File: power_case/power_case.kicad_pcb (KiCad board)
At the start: 2 copper layers, 22 x 27.1 mm, 4 parts, among them P1 CONN_01X05, P2 CONN_01X03, Q1 Q_NJFET_DGS, Q2 Q_NJFET_DGS

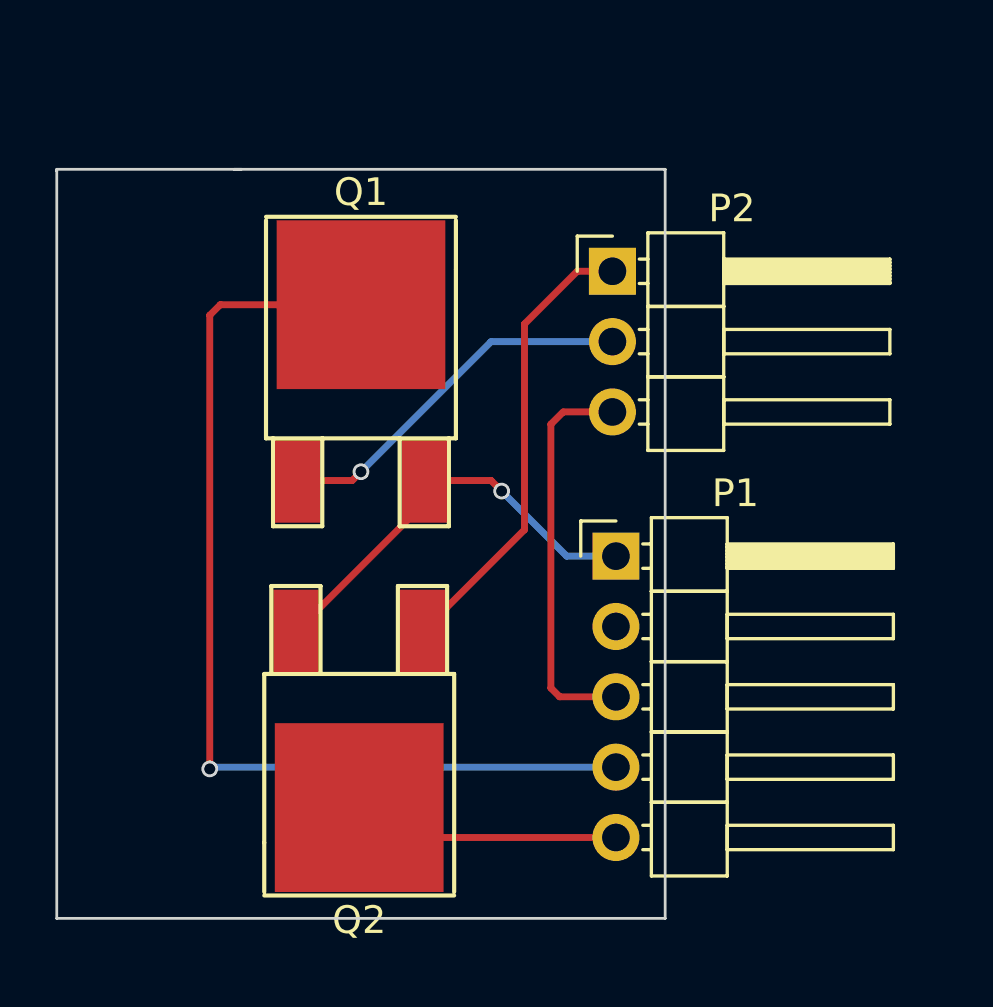
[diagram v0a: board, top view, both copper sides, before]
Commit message: addition of pin labels to power case
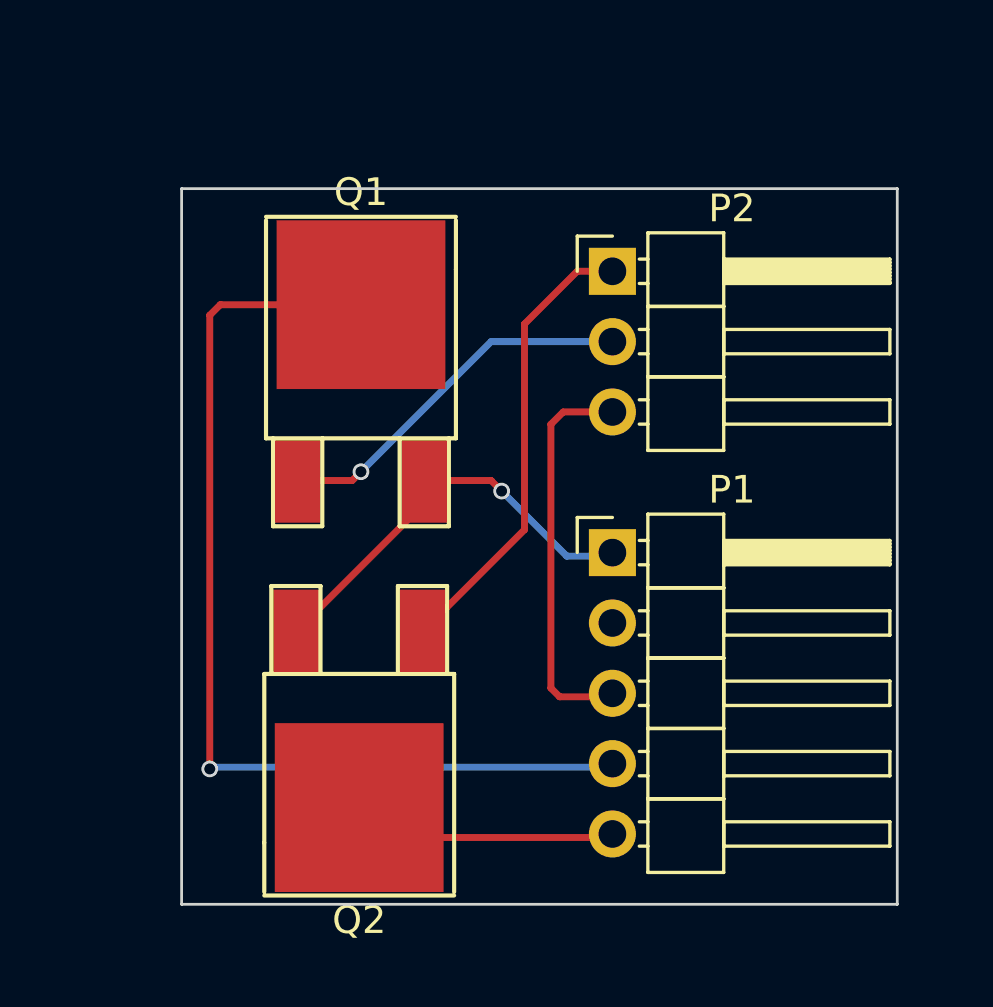
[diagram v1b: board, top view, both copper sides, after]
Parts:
- added G***: LOGO, robosub_footprints:robosub_logo-medium, B.Cu at (152.0, 71.2)
- moved P1 0.18 mm to (160.1, 79.6)
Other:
- board size 22 x 27.1 mm -> 25.8 x 25.8 mm
- board text added: "B_Coil"
- board text added: "B_Voltage"
- board text added: "Battery Voltage"
- board text added: "Bulkhead Voltage"
- board text added: "Daniel Goto"
- board text added: "GND"
- board text added: "Power Management"
- board text added: "RS17"
- board text added: "T_Coil"

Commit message: changed pin labels and position
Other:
- board text added: "Battery V+"
- board text added: "Bcoil"
- board text added: "Bgate"
- board text added: "Tcoil"
- board text removed: "B_Coil"
- board text removed: "B_Voltage"
- board text removed: "Battery Voltage"
- board text removed: "Bulkhead Voltage"
- board text removed: "T_Coil"
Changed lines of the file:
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@@
       (xy -1.188084 0.408) (xy -1.187006 0.406096)) (layer B.SilkS) (width 0.01))
   )
-  (gr_text B_Coil (at 157.1625 87.249) (layer B.SilkS)
-    (effects (font (size 0.508 0.508) (thickness 0.0762)))
+  (gr_text Bcoil (at 157.1625 87.249) (layer B.SilkS)
+    (effects (font (size 0.508 0.508) (thickness 0.0762)) (justify mirror))
   )
-  (gr_text "T_Coil\n" (at 157.0355 89.916) (layer B.SilkS)
-    (effects (font (size 0.508 0.508) (thickness 0.0762)))
+  (gr_text Tcoil (at 157.0355 89.916) (layer B.SilkS)
+    (effects (font (size 0.508 0.508) (thickness 0.0762)) (justify mirror))
   )
-  (gr_text "Bulkhead  Voltage" (at 155.194 84.709) (layer B.SilkS)
-    (effects (font (size 0.508 0.508) (thickness 0.0762)))
+  (gr_text "Bgate\n" (at 156.5275 84.582) (layer B.SilkS)
+    (effects (font (size 0.508 0.508) (thickness 0.0762)) (justify mirror))
   )
-  (gr_text "Battery Voltage" (at 155.5115 82.1055) (layer B.SilkS)
-    (effects (font (size 0.508 0.508) (thickness 0.0762)))
+  (gr_text "Battery V+\n" (at 156.718 82.169) (layer B.SilkS)
+    (effects (font (size 0.508 0.508) (thickness 0.0762)) (justify mirror))
   )
   (gr_text GND (at 157.6705 79.6925) (layer B.SilkS)
-    (effects (font (size 0.508 0.508) (thickness 0.0762)))
+    (effects (font (size 0.508 0.508) (thickness 0.0762)) (justify mirror))
   )
-  (gr_text B_Voltage (at 157.0355 74.4855) (layer B.SilkS)
-    (effects (font (size 0.508 0.508) (thickness 0.0762)))
+  (gr_text "Bgate\n" (at 157.0355 74.4855) (layer B.SilkS)
+    (effects (font (size 0.508 0.508) (thickness 0.0762)) (justify mirror))
   )
-  (gr_text B_Coil (at 157.48 72.009) (layer B.SilkS)
-    (effects (font (size 0.508 0.508) (thickness 0.0762)))
+  (gr_text "Bcoil\n" (at 156.464 72.0725) (layer B.SilkS)
+    (effects (font (size 0.508 0.508) (thickness 0.0762)) (justify mirror))
   )
-  (gr_text "T_Coil\n" (at 157.4165 69.469) (layer B.SilkS)
-    (effects (font (size 0.508 0.508) (thickness 0.0762)))
+  (gr_text "Tcoil\n" (at 156.6545 69.4055) (layer B.SilkS)
+    (effects (font (size 0.508 0.508) (thickness 0.0762)) (justify mirror))
   )
   (gr_text "Daniel Goto" (at 151.13 77.851) (layer B.SilkS)
-    (effects (font (size 1.016 1.016) (thickness 0.127)))
+    (effects (font (size 1.016 1.016) (thickness 0.127)) (justify mirror))
   )
   (gr_text RS17 (at 151.003 75.946) (layer B.SilkS)
-    (effects (font (size 1.5 1.5) (thickness 0.3)))
+    (effects (font (size 1.5 1.5) (thickness 0.3)) (justify mirror))
   )
   (gr_text "Power Management\n" (at 151.003 74.295) (layer B.SilkS)

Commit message: Reloaded netlist
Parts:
- removed P2: CONN_01X03, Pin_Headers:Pin_Header_Angled_1x03_Pitch2.54mm
- added R1: R, Resistors_SMD:R_0402, F.Cu at (163.5, 91.2)
- added R2: R, Resistors_SMD:R_0402, F.Cu at (155.4, 86.6)
- P1: value CONN_01X05 -> CONN_02X03; footprint Pin_Headers:Pin_Header_Angled_1x05_Pitch2.54mm -> Pin_Headers:Pin_Header_Angled_2x03_Pitch2.54mm
- moved Q1 12.5 mm to (151.3, 89.5)
- moved Q2 10.4 mm to (160.3, 87.0), turned to 270 degrees
- moved P1 0.60 mm to (159.8, 79.1), turned to 90 degrees
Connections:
- P1 pad 1: GND -> bCoil
- P1 pad 2: Battery+ -> Net-(P1-Pad2)
- P1 pad 3: Bulkhead+ -> Tcoil
- Q2 pad 1: ThrusterCoil -> Tcoil
- Q2 pad 2: Net-(P1-Pad5) -> Net-(P1-Pad2)
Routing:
- net Net-(P1-Pad2): track 0.00 -> 24.8 mm
- net GND: track 15.4 -> 36.7 mm, vias 1 -> 2
- net ThrusterCoil: track 16.6 -> 0.00 mm
- net Bulkhead+: track 14.4 -> 0.00 mm
- net Net-(P1-Pad4): track 36.7 -> 23.2 mm, vias 1 -> 0
- net Net-(P1-Pad5): track 9.72 -> 0.00 mm
- net Tcoil: track 0.00 -> 6.40 mm
- net bCoil: track 13.4 -> 16.4 mm
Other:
- board text added: "Bcoil from | Tcoil Bulkhead | toRelay"
- board text added: "Tcoil from | bCoil Bulkhead | toRelay"
- board text added: "Unused | GND"
- board text removed: "Battery V+"
- board text removed: "Bcoil"
- board text removed: "Bgate"
- board text removed: "GND"
- board text removed: "Tcoil"

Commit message: more finalization
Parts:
- G***: moved to F.Cu
- P1: footprint Pin_Headers:Pin_Header_Angled_2x03_Pitch2.54mm -> robosub_footprints:Pin_Header_Angled_2x03_Pitch2.54mm_new
- R1, R2: value R -> 5k; footprint Resistors_SMD:R_0402 -> Resistors_SMD:R_0805_HandSoldering
- moved R1 6.24 mm to (157.3, 91.2), turned to 0 degrees
- moved P1 4.45 mm to (159.9, 74.7)
- moved G*** 3.31 mm to (150.8, 68.1), turned to 0 degrees
- moved R2 1.16 mm to (156.2, 85.7)
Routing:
- net Net-(P1-Pad2): track 24.8 -> 33.6 mm, vias 0 -> 4
- net bCoil: track 16.4 -> 20.8 mm
- net Tcoil: track 6.40 -> 10.9 mm
- net GND: track 36.7 -> 38.8 mm
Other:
- board size 25.8 x 25.8 mm -> 25.8 x 30.6 mm
- board text added: "Bcoil | Tcoil"
- board text added: "Tcoil | bCoil"
- board text added: "X | GND"
- board text removed: "Bcoil from | Tcoil Bulkhead | toRelay"
- board text removed: "Tcoil from | bCoil Bulkhead | toRelay"
- board text removed: "Unused | GND"
